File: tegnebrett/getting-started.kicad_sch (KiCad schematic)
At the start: 51 parts, among them J1 FH12-45S-0.5SH55, J2 FH12-6S-1SH55, J3 Conn_ST_STDC14, J5 MCU_Header_Pin, J8 USB-A1HSW6, SW1 SW_Push, SW2 SW_Push, SW3 Undo, SW4 Reset, SW5 MCU_Button, U5 STM32U5G7VJTxQ, Y1 48MHz

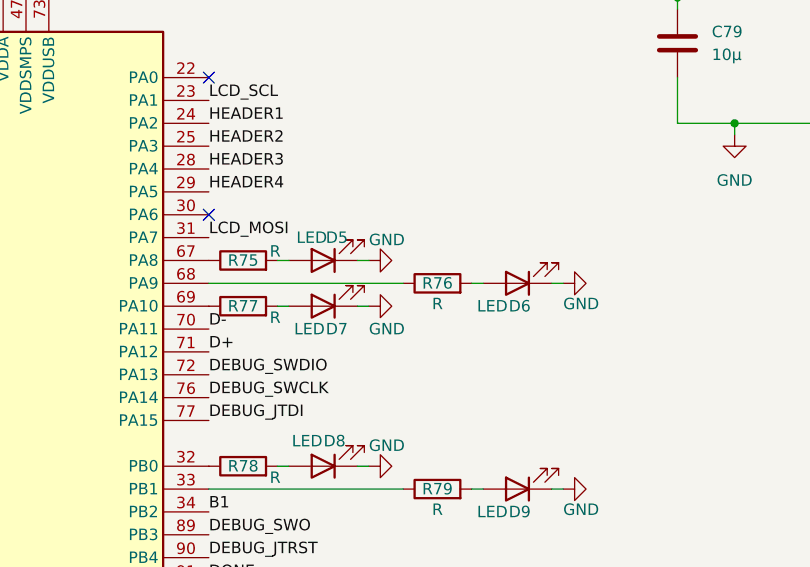
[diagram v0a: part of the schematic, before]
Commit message: refactor: remove unused LEDs
We have too many LEDs.
We're thinking two LEDs for the MCU and two LEDs for the FPGA.
Additionally have one Green LED at power supply to indicate that power
is on.
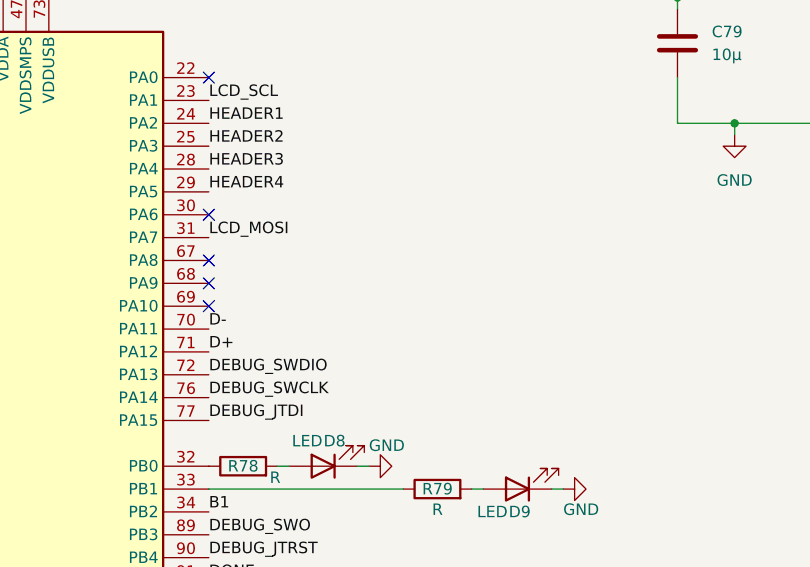
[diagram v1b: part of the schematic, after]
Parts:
- removed D5, D6, D7: LED, tegnebrett_modules:LED_J-SERIES_3030_CRW-M, symbol Device:LED
- removed R75, R76, R77: R, symbol Device:R
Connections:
- no-connect marks 14 -> 17

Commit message: refactor: use new LED variants.
These have a supply voltage of 2V, and they have a current of 5mA.
These are nice numbers which gives a required resistance of 260 Ohm,
assuming a supply voltage of 3.3V

We're using 270 Ohms though, as 260 is not standard.
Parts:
- D8, D9: footprint tegnebrett_modules:LED_J-SERIES_3030_CRW-M -> tegnebrett_modules:LED_LTST-C193KGKT-5A_LTO-M
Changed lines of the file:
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@@
 			)
 		)
-		(property "Footprint" "tegnebrett_modules:LED_J-SERIES_3030_CRW-M"
+		(property "Footprint" "tegnebrett_modules:LED_LTST-C193KGKT-5A_LTO-M"
 			(at 157.48 96.52 0)
 			(effects
@@
 			)
 		)
-		(property "Footprint" "tegnebrett_modules:LED_J-SERIES_3030_CRW-M"
+		(property "Footprint" "tegnebrett_modules:LED_LTST-C193KGKT-5A_LTO-M"
 			(at 179.07 99.06 0)
 			(effects

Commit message: feat: add LED to 3.3V from power supply, and set resistors to 270ohm.
Additionally add footprints to these resistors which *did not* yet have
a footprint (because their resistor values were not determined yet).
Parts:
- R78, R79: value R -> 270; footprint (none) -> Resistor_SMD:R_0805_2012Metric_Pad1.20x1.40mm_HandSolder
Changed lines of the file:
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@@
 			)
 		)
-		(property "Value" "R"
+		(property "Value" "270"
 			(at 152.146 97.79 90)
 			(effects
@@
 			)
 		)
-		(property "Footprint" ""
+		(property "Footprint" "Resistor_SMD:R_0805_2012Metric_Pad1.20x1.40mm_HandSolder"
 			(at 148.59 98.298 90)
 			(effects
@@
 			)
 		)
-		(property "Value" "R"
+		(property "Value" "270"
 			(at 170.18 101.346 90)
 			(effects
@@
 			)
 		)
-		(property "Footprint" ""
+		(property "Footprint" "Resistor_SMD:R_0805_2012Metric_Pad1.20x1.40mm_HandSolder"
 			(at 170.18 100.838 90)
 			(effects

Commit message: feat: add 15V power jack symbol and import to schematic
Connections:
- no-connect marks 17 -> 19
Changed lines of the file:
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@@
+	)
+	(no_connect
+		(at 144.78 149.86)
+	)
+	(no_connect
+		(at 144.78 147.32)
 	)
 	(no_connect

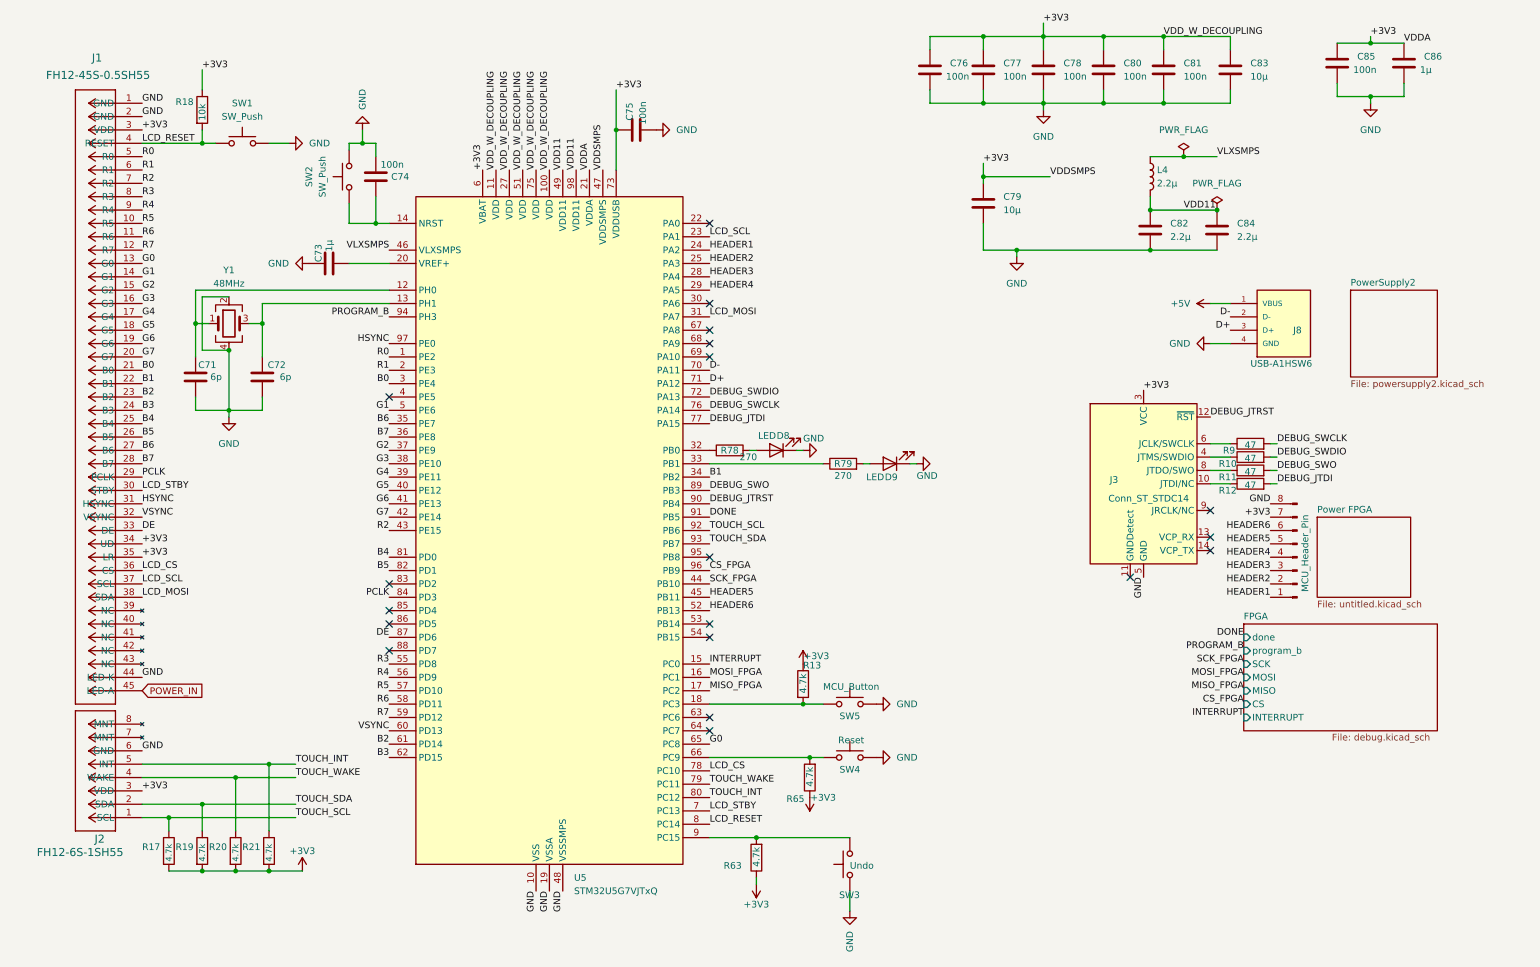
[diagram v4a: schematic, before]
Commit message: refactor: re-annotate schematic labels
References for schematic capacitors (for example C74 -> C2), etc.
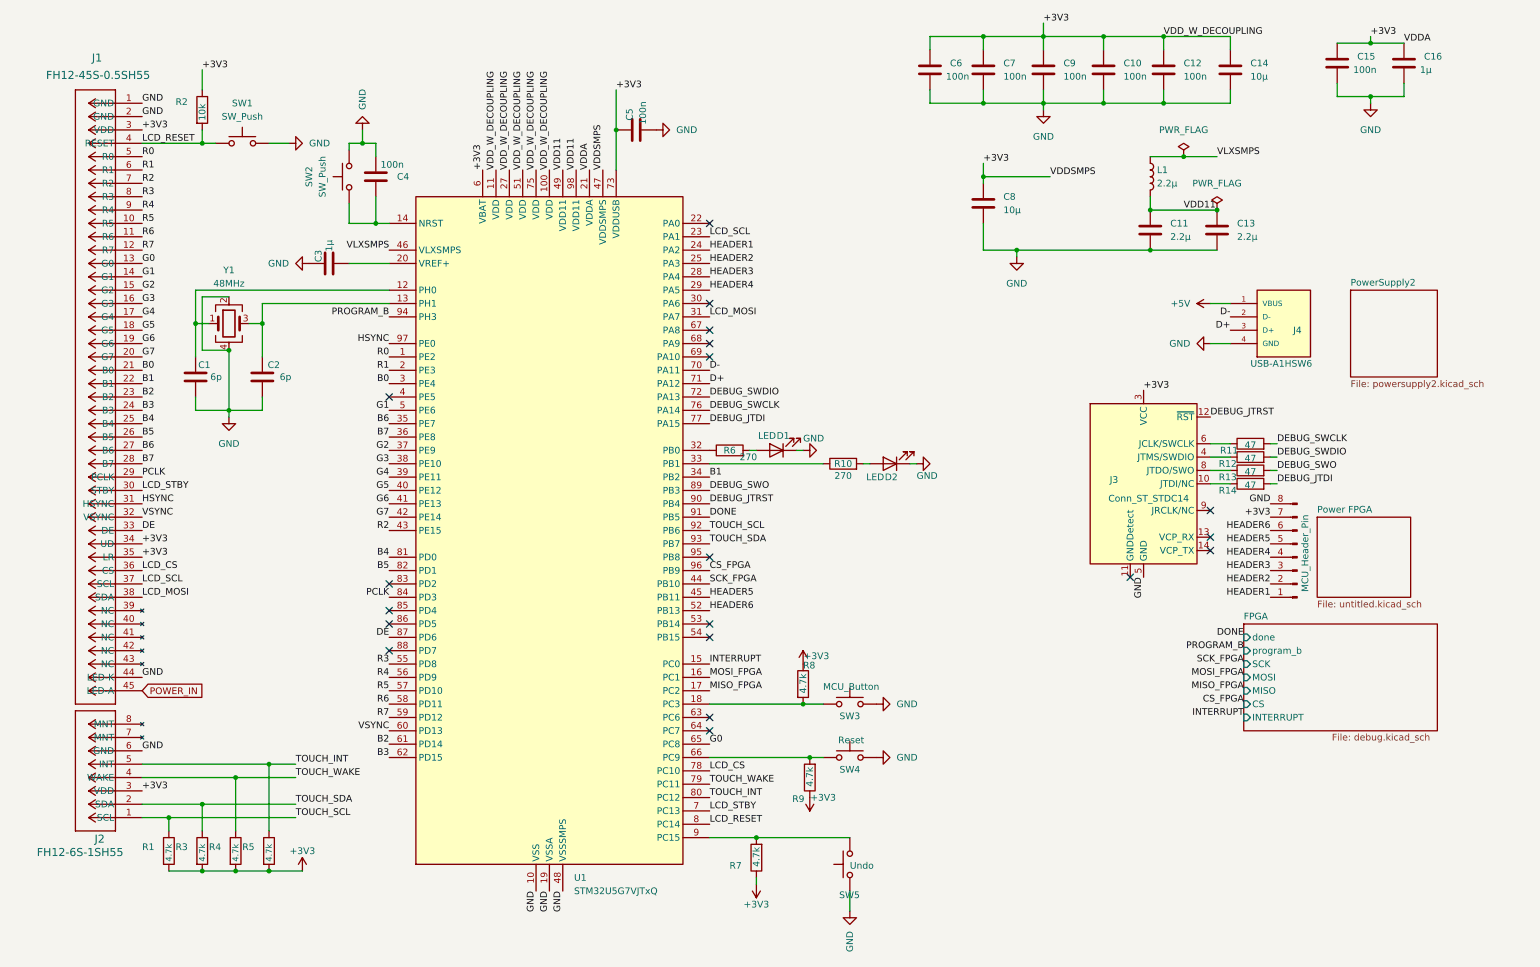
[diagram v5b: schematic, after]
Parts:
- renumbered C71 to C1, C80 to C10, C82 to C11, C81 to C12, C84 to C13, C83 to C14, C85 to C15, C86 to C16, C72 to C2, C73 to C3, C74 to C4, C75 to C5, C76 to C6, C77 to C7, C79 to C8, C78 to C9, D8 to D1, D9 to D2, J8 to J4, L4 to L1, R17 to R1, R79 to R10, R9 to R11, R10 to R12, R11 to R13, R12 to R14, R18 to R2, R19 to R3, R20 to R4, R21 to R5, R78 to R6, R63 to R7, R13 to R8, R65 to R9, SW5 to SW3, SW3 to SW5, U5 to U1

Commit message: schematic: some smaller updates
I am not entirely sure what was updated, but surely not antyhing huge.
From the diff we can read that it's perhaps the symbols which got an
update.
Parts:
- J4: footprint tegnebrett_modules:OST_USB-A1HSW6 -> USB-A1HSW6:OST_USB-A1HSW6
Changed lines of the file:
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@@
 			)
 		)
-		(property "Footprint" "tegnebrett_modules:OST_USB-A1HSW6"
+		(property "Footprint" "USB-A1HSW6:OST_USB-A1HSW6"
 			(at 254 73.66 0)
 			(effects
